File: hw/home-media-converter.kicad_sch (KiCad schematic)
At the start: 84 parts, among them J1 0826-1X1T-32-F, J2 Conn_01x04_Male, J3 Conn_01x03, J4 Conn_01x03, J5 Conn_01x03, J6 RJ45_LED_Shielded, SW1 SW_Push, U1 KSZ9131RNXC-TR, U2 STM32F030F4Px, U3 DP83TG720RWRHATQ1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

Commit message: Bigger components on MDI
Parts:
- C16: footprint Capacitor_SMD:C_0402_1005Metric -> Capacitor_SMD:C_1206_3216Metric
- R38: footprint Resistor_SMD:R_0402_1005Metric -> Resistor_SMD:R_0805_2012Metric
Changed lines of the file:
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@@
       (effects (font (size 1.27 1.27)) (justify left))
     )
-    (property "Footprint" "Capacitor_SMD:C_0402_1005Metric" (at 346.4052 226.06 0)
+    (property "Footprint" "Capacitor_SMD:C_1206_3216Metric" (at 346.4052 226.06 0)
       (effects (font (size 1.27 1.27)) hide)
     )
@@
       (effects (font (size 1.27 1.27)) (justify left))
     )
-    (property "Footprint" "Resistor_SMD:R_0402_1005Metric" (at 351.282 222.25 90)
+    (property "Footprint" "Resistor_SMD:R_0805_2012Metric" (at 351.282 222.25 90)
       (effects (font (size 1.27 1.27)) hide)
     )

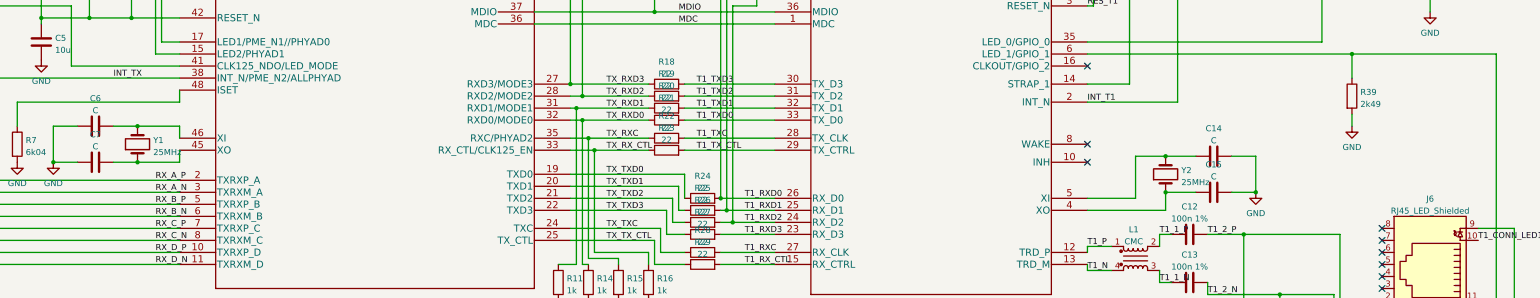
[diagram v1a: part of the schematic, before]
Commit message: Set missing part values, create BOM
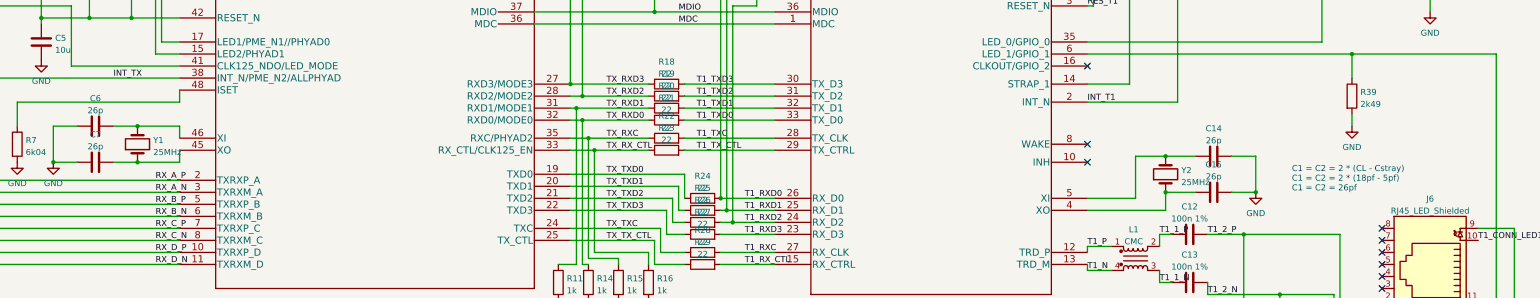
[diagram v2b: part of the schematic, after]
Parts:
- C14, C15, C6, C7: value C -> 26p
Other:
- note added: "C1 = C2 = 2 * (CL - Cstray) C1 = C2 = 2 * (18pf - 5pf) C1 = C2 = 26pf"
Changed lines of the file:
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@@
+    (effects (font (size 1.27 1.27)) (justify left bottom))
+  )
+  (text "C1 = C2 = 2 * (CL - Cstray)\nC1 = C2 = 2 * (18pf - 5pf)\nC1 = C2 = 26pf"
+    (at 355.6 179.07 0)
     (effects (font (size 1.27 1.27)) (justify left bottom))
   )
@@
       (effects (font (size 1.27 1.27)))
     )
-    (property "Value" "C" (at 102.87 161.7781 90)
+    (property "Value" "26p" (at 102.87 161.7781 90)
       (effects (font (size 1.27 1.27)))
     )
@@
       (effects (font (size 1.27 1.27)))
     )
-    (property "Value" "C" (at 339.09 168.1281 90)
+    (property "Value" "26p" (at 339.09 168.1281 90)
       (effects (font (size 1.27 1.27)))
     )
@@
       (effects (font (size 1.27 1.27)))
     )
-    (property "Value" "C" (at 339.09 175.7481 90)
+    (property "Value" "26p" (at 339.09 175.7481 90)
       (effects (font (size 1.27 1.27)))
     )
@@
       (effects (font (size 1.27 1.27)))
     )
-    (property "Value" "C" (at 102.87 169.3981 90)
-      (effects (font (size 1.27 1.27)))
-    )
+    (property "Value" "26p" (at 102.87 169.3981 90)
+      (effects (font (size 1.27 1.27)))
+    )

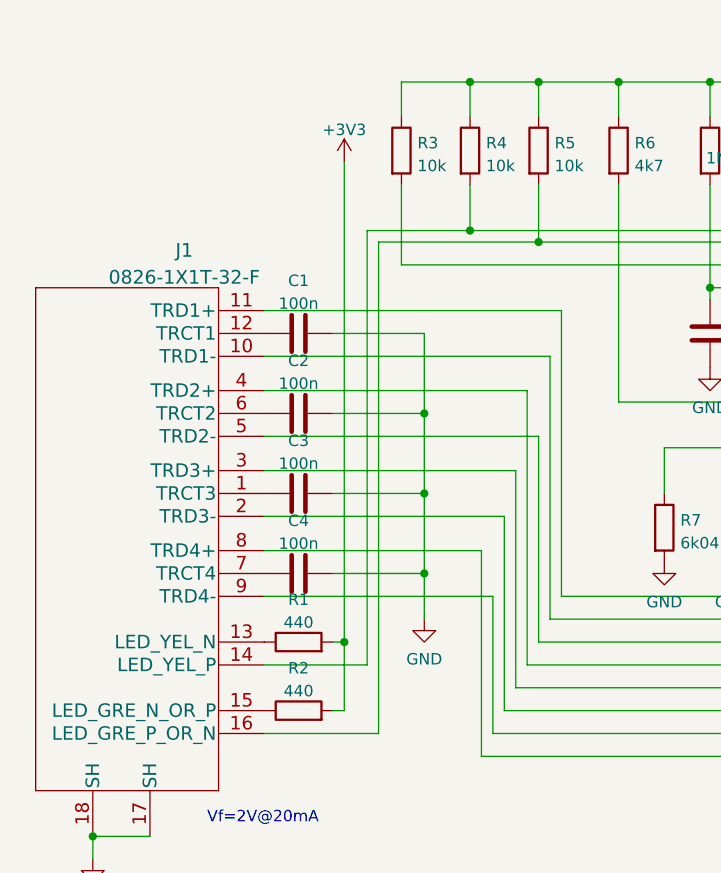
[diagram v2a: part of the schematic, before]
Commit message: Fix MagJack LED polarity
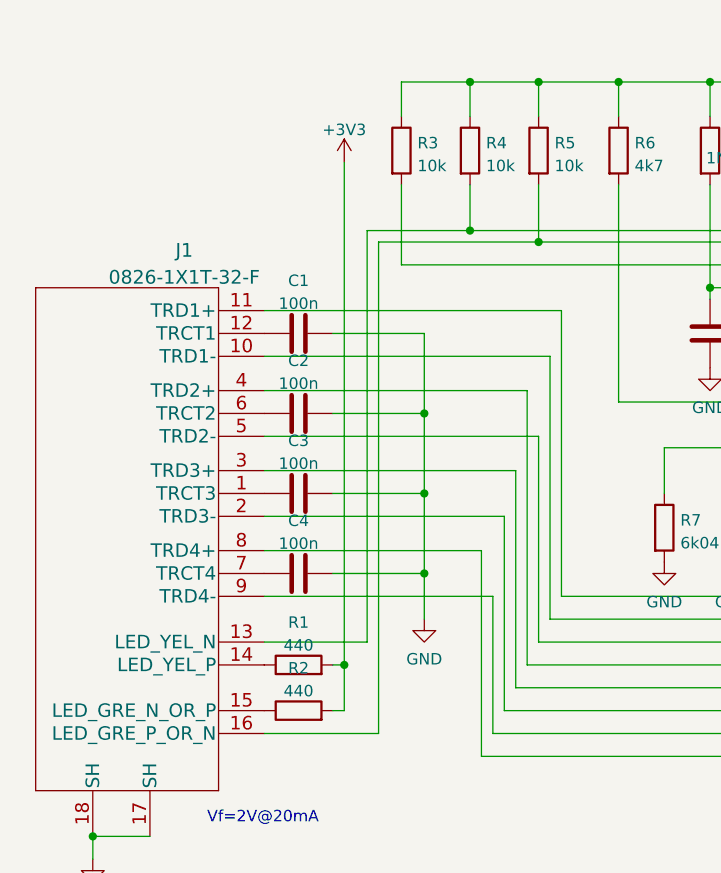
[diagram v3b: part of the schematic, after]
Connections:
- net at J1.13 (LED_YEL_N): now also R4.2, U1.17 (LED1/PME_N1//PHYAD0); no longer R1.1
- new net: J1.14 (LED_YEL_P), R1.1
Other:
- moved on the sheet: R1
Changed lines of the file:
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@@
   (junction (at 43.18 255.27) (diameter 0) (color 0 0 0 0)
   )
-  (junction (at 50.8 181.61) (diameter 0) (color 0 0 0 0)
-  )
   (junction (at 207.01 130.81) (diameter 0) (color 0 0 0 0)
   )
@@
   )
   (junction (at 35.56 255.27) (diameter 0) (color 0 0 0 0)
+  )
+  (junction (at 50.8 184.15) (diameter 0) (color 0 0 0 0)
   )
   (junction (at 59.69 173.99) (diameter 0) (color 0 0 0 0)
@@
     (stroke (width 0) (type default))
   )
-  (wire (pts (xy 49.53 181.61) (xy 50.8 181.61))
-    (stroke (width 0) (type default))
-  )
   (wire (pts (xy 242.57 139.7) (xy 237.49 139.7))
     (stroke (width 0) (type default))
@@
     (stroke (width 0) (type default))
   )
-  (wire (pts (xy 50.8 181.61) (xy 50.8 128.27))
-    (stroke (width 0) (type default))
-  )
   (wire (pts (xy 313.69 123.19) (xy 313.69 128.27))
     (stroke (width 0) (type default))
@@
     (stroke (width 0) (type default))
   )
-  (wire (pts (xy 53.34 184.15) (xy 53.34 135.89))
-    (stroke (width 0) (type default))
-  )
   (wire (pts (xy 54.61 137.16) (xy 72.39 137.16))
     (stroke (width 0) (type default))
@@
     (stroke (width 0) (type default))
   )
+  (wire (pts (xy 50.8 184.15) (xy 50.8 189.23))
+    (stroke (width 0) (type default))
+  )
   (wire (pts (xy 328.93 171.45) (xy 335.28 171.45))
     (stroke (width 0) (type default))
@@
     (stroke (width 0) (type default))
   )
-  (wire (pts (xy 41.91 184.15) (xy 53.34 184.15))
-    (stroke (width 0) (type default))
-  )
   (wire (pts (xy 105.41 60.96) (xy 110.49 60.96))
     (stroke (width 0) (type default))
@@
     (stroke (width 0) (type default))
   )
+  (wire (pts (xy 53.34 135.89) (xy 53.34 181.61))
+    (stroke (width 0) (type default))
+  )
   (wire (pts (xy 236.22 182.88) (xy 246.38 182.88))
     (stroke (width 0) (type default))
@@
     (stroke (width 0) (type default))
   )
-  (wire (pts (xy 50.8 189.23) (xy 50.8 181.61))
+  (wire (pts (xy 50.8 128.27) (xy 50.8 184.15))
     (stroke (width 0) (type default))
   )
@@
   )
   (wire (pts (xy 200.66 201.93) (xy 207.01 201.93))
+    (stroke (width 0) (type default))
+  )
+  (wire (pts (xy 53.34 181.61) (xy 41.91 181.61))
+    (stroke (width 0) (type default))
+  )
+  (wire (pts (xy 49.53 184.15) (xy 50.8 184.15))
     (stroke (width 0) (type default))
   )
@@
     )
   )
-  (symbol (lib_id "Device:R") (at 45.72 181.61 90) (unit 1)
-    (in_bom yes) (on_board yes) (dnp no) (fields_autoplaced)
-    (property "Reference" "R1" (at 45.72 176.8942 90)
-      (effects (font (size 1.27 1.27)))
-    )
-    (property "Value" "440" (at 45.72 179.4311 90)
-      (effects (font (size 1.27 1.27)))
-    )
-    (property "Footprint" "Resistor_SMD:R_0402_1005Metric" (at 45.72 183.388 90)
-      (effects (font (size 1.27 1.27)) hide)
-    )
-    (property "Datasheet" "~" (at 45.72 181.61 0)
-      (effects (font (size 1.27 1.27)) hide)
-    )
+  (symbol (lib_id "Device:R") (at 45.72 184.15 90) (unit 1)
+    (in_bom yes) (on_board yes) (dnp no) (fields_autoplaced)
+    (property "Reference" "R1" (at 45.72 179.4342 90)
+      (effects (font (size 1.27 1.27)))
+    )
+    (property "Value" "440" (at 45.72 181.9711 90)
+      (effects (font (size 1.27 1.27)))
+    )
+    (property "Footprint" "Resistor_SMD:R_0402_1005Metric" (at 45.72 185.928 90)
+      (effects (font (size 1.27 1.27)) hide)
+    )
+    (property "Datasheet" "~" (at 45.72 184.15 0)
+      (effects (font (size 1.27 1.27)) hide)
+    )
